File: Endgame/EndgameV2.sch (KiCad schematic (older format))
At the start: 160 parts, among them J1 OLED, SW1 Rotary_Encoder, SW2 SW_PUSH, U1 ATmega32U4-AU, U2 ai03-locallib_PRTR5V0U2X, Y1 Crystal_GND24_Small

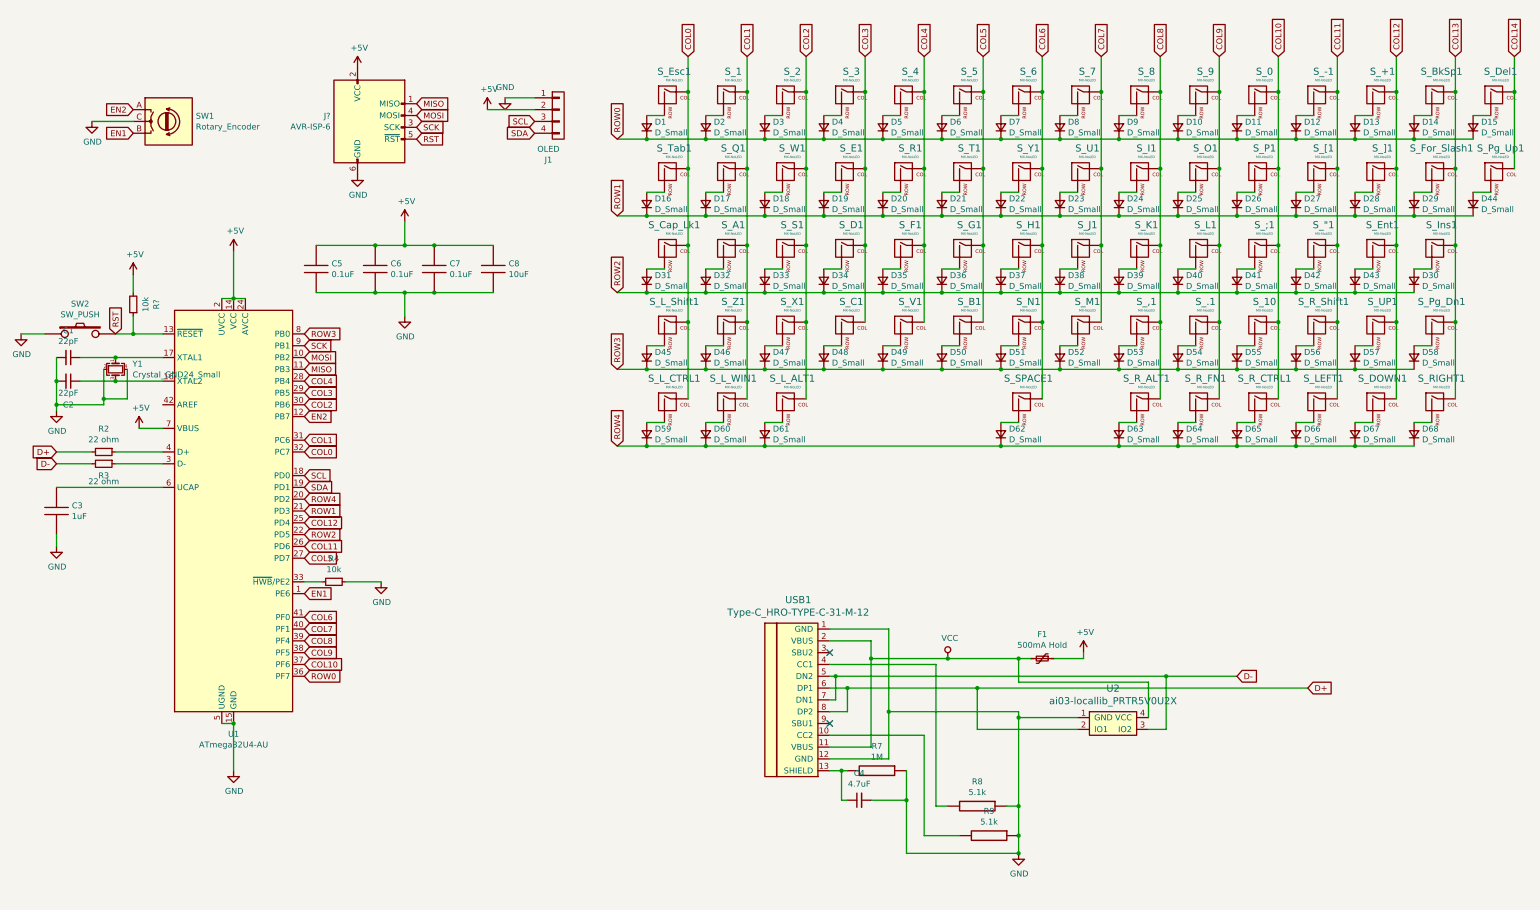
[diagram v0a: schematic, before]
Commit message: redrew key matrix
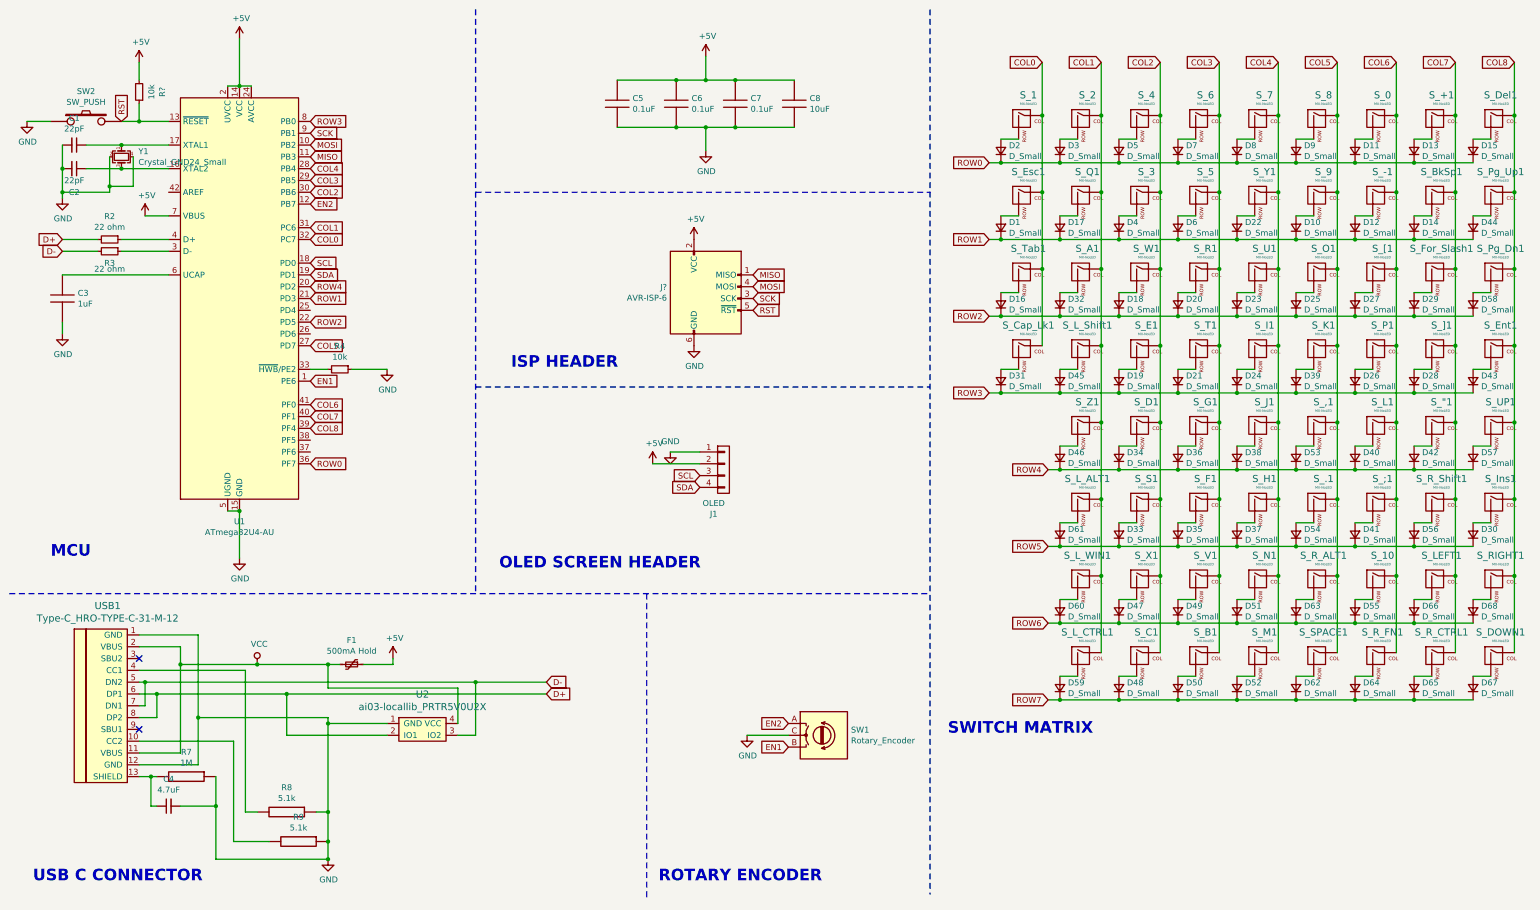
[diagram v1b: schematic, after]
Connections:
- net COL14 is gone; now on net COL8: S_Del1.1 (COL), S_Pg_Up1.1 (COL)
- net COL0: now also S_1.1 (COL); no longer S_L_CTRL1.1 (COL), S_L_Shift1.1 (COL)
- net COL1: now also S_2.1 (COL), S_L_ALT1.1 (COL), S_L_CTRL1.1 (COL), S_L_Shift1.1 (COL); no longer S_1.1 (COL)
- net COL2: now also S_3.1 (COL), S_4.1 (COL), S_C1.1 (COL), S_D1.1 (COL), S_E1.1 (COL); no longer S_2.1 (COL), S_L_ALT1.1 (COL)
- net COL3: now also S_5.1 (COL), S_6.1 (COL), S_B1.1 (COL), S_F1.1 (COL), S_G1.1 (COL), S_R1.1 (COL), S_T1.1 (COL), S_V1.1 (COL); no longer S_3.1 (COL), S_C1.1 (COL), S_D1.1 (COL), S_E1.1 (COL)
- net COL4: now also S_7.1 (COL), S_H1.1 (COL), S_I1.1 (COL), S_J1.1 (COL), S_M1.1 (COL), S_N1.1 (COL), S_U1.1 (COL), S_Y1.1 (COL); no longer S_4.1 (COL), S_F1.1 (COL), S_R1.1 (COL), S_V1.1 (COL)
- net COL5: now also S_,1.1 (COL), S_.1.1 (COL), S_8.1 (COL), S_9.1 (COL), S_K1.1 (COL), S_O1.1 (COL), S_R_ALT1.1 (COL), S_SPACE1.1 (COL); no longer S_5.1 (COL), S_B1.1 (COL), S_G1.1 (COL), S_T1.1 (COL)
- net COL6: now also S_-1.1 (COL), S_0.1 (COL), S_10.1 (COL), S_;1.1 (COL), S_L1.1 (COL), S_P1.1 (COL), S_R_FN1.1 (COL), S_[1.1 (COL); no longer S_6.1 (COL), S_H1.1 (COL), S_N1.1 (COL), S_SPACE1.1 (COL), S_Y1.1 (COL)
- net COL7: now also S_"1.1 (COL), S_+1.1 (COL), S_BkSp1.1 (COL), S_For_Slash1.1 (COL), S_LEFT1.1 (COL), S_R_CTRL1.1 (COL), S_R_Shift1.1 (COL), S_]1.1 (COL); no longer S_7.1 (COL), S_J1.1 (COL), S_M1.1 (COL), S_U1.1 (COL)
- net COL8: now also S_DOWN1.1 (COL), S_Ent1.1 (COL), S_Ins1.1 (COL), S_Pg_Dn1.1 (COL), S_RIGHT1.1 (COL), S_UP1.1 (COL); no longer S_,1.1 (COL), S_8.1 (COL), S_I1.1 (COL), S_K1.1 (COL), S_R_ALT1.1 (COL)
- net ROW0: no longer D1.1 (K), D10.1 (K), D12.1 (K), D14.1 (K), D4.1 (K), D6.1 (K)
- net ROW1: now also D1.1 (K), D10.1 (K), D12.1 (K), D14.1 (K), D4.1 (K), D6.1 (K); no longer D16.1 (K), D18.1 (K), D19.1 (K), D20.1 (K), D21.1 (K), D23.1 (K), D24.1 (K), D25.1 (K), D26.1 (K), D27.1 (K), D28.1 (K), D29.1 (K)
- net ROW2: now also D16.1 (K), D18.1 (K), D20.1 (K), D23.1 (K), D25.1 (K), D27.1 (K), D29.1 (K), D58.1 (K); no longer D30.1 (K), D31.1 (K), D33.1 (K), D34.1 (K), D35.1 (K), D36.1 (K), D37.1 (K), D38.1 (K), D39.1 (K), D40.1 (K), D41.1 (K), D42.1 (K), D43.1 (K)
- net ROW3: now also D19.1 (K), D21.1 (K), D24.1 (K), D26.1 (K), D28.1 (K), D31.1 (K), D39.1 (K), D43.1 (K); no longer D46.1 (K), D47.1 (K), D48.1 (K), D49.1 (K), D50.1 (K), D51.1 (K), D52.1 (K), D53.1 (K), D54.1 (K), D55.1 (K), D56.1 (K), D57.1 (K), D58.1 (K)
- net ROW4: now also D34.1 (K), D36.1 (K), D38.1 (K), D40.1 (K), D42.1 (K), D46.1 (K), D53.1 (K), D57.1 (K); no longer D59.1 (K), D60.1 (K), D61.1 (K), D62.1 (K), D63.1 (K), D64.1 (K), D65.1 (K), D66.1 (K), D67.1 (K), D68.1 (K)
- removed net COL10: S_0.1 (COL), S_10.1 (COL), S_;1.1 (COL), S_P1.1 (COL), S_R_CTRL1.1 (COL), U1.37 (PF6)
- removed net COL11: S_"1.1 (COL), S_-1.1 (COL), S_LEFT1.1 (COL), S_R_Shift1.1 (COL), S_[1.1 (COL), U1.26 (PD6)
- removed net COL12: S_+1.1 (COL), S_DOWN1.1 (COL), S_Ent1.1 (COL), S_UP1.1 (COL), S_]1.1 (COL), U1.25 (PD4)
- removed net COL13: S_BkSp1.1 (COL), S_For_Slash1.1 (COL), S_Ins1.1 (COL), S_Pg_Dn1.1 (COL), S_RIGHT1.1 (COL)
- removed net COL9: S_.1.1 (COL), S_9.1 (COL), S_L1.1 (COL), S_O1.1 (COL), S_R_FN1.1 (COL), U1.38 (PF5)
- new net ROW5: D30.1 (K), D33.1 (K), D35.1 (K), D37.1 (K), D41.1 (K), D54.1 (K), D56.1 (K), D61.1 (K)
- new net ROW6: D47.1 (K), D49.1 (K), D51.1 (K), D55.1 (K), D60.1 (K), D63.1 (K), D66.1 (K), D68.1 (K)
- new net ROW7: D48.1 (K), D50.1 (K), D52.1 (K), D59.1 (K), D62.1 (K), D64.1 (K), D65.1 (K), D67.1 (K)
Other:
- note added: "ISP HEADER"
- note added: "MCU"
- note added: "OLED SCREEN HEADER"
- note added: "ROTARY ENCODER"
- note added: "SWITCH MATRIX"
- note added: "USB C CONNECTOR"
- moved on the sheet: C1, C2, C3, C4, C5, C6, C7, C8, D1, D10, D11, D12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

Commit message: USB retrace
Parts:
- J2: renamed from J?; footprint (none) -> Keebio-Parts:ICSP-Header
- gave numbers to parts that had none: 1
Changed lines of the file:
@@
 $EndComp
 Wire Wire Line
-	2400 750  2400 1150
+	2300 750  2300 1150
 Wire Wire Line
 	2500 1150 2400 1150
@@
 L power:+5V #PWR0108
 U 1 1 5DE865F8
-P 2400 750
-F 0 "#PWR0108" H 2400 600 50  0001 C CNN
-F 1 "+5V" H 2415 923 50  0000 C CNN
-F 2 "" H 2400 750 50  0001 C CNN
-F 3 "" H 2400 750 50  0001 C CNN
-	1    2400 750
+P 2300 750
+F 0 "#PWR0108" H 2300 600 50  0001 C CNN
+F 1 "+5V" H 2315 923 50  0000 C CNN
+F 2 "" H 2300 750 50  0001 C CNN
+F 3 "" H 2300 750 50  0001 C CNN
+	1    2300 750
 	1    0    0    -1
 $EndComp
@@
 	1400 2550 1800 2550
 $Comp
-L power:+5V #PWR?
+L power:+5V #PWR0106
 U 1 1 5DF42376
 P 5900 4350
-F 0 "#PWR?" H 5900 4200 50  0001 C CNN
+F 0 "#PWR0106" H 5900 4200 50  0001 C CNN
 F 1 "+5V" H 5915 4523 50  0000 C CNN
 F 2 "" H 5900 4350 50  0001 C CNN
@@
 	5900 4350 6300 4350
 $Comp
-L Device:R_Small R?
+L Device:R_Small R1
 U 1 1 5DE94258
 P 1550 1200
-F 0 "R?" V 1354 1200 50  0000 C CNN
+F 0 "R1" V 1354 1200 50  0000 C CNN
 F 1 "10k" V 1445 1200 50  0000 C CNN
 F 2 "Resistor_SMD:R_0805_2012Metric" H 1550 1200 50  0001 C CNN
@@
 	1550 1450 1800 1450
 $Comp
-L power:+5V #PWR?
+L power:+5V #PWR0107
 U 1 1 5DE97BB7
 P 1550 950
-F 0 "#PWR?" H 1550 800 50  0001 C CNN
+F 0 "#PWR0107" H 1550 800 50  0001 C CNN
 F 1 "+5V" H 1565 1123 50  0000 C CNN
 F 2 "" H 1550 950 50  0001 C CNN
@@
 	1550 1100 1550 950
 $Comp
-L Connector:AVR-ISP-6 J?
+L Connector:AVR-ISP-6 J2
 U 1 1 5DF23484
 P 6350 2950
-F 0 "J?" H 6021 3046 50  0000 R CNN
+F 0 "J2" H 6021 3046 50  0000 R CNN
 F 1 "AVR-ISP-6" H 6021 2955 50  0000 R CNN
-F 2 "" V 6100 3000 50  0001 C CNN
+F 2 "Keebio-Parts:ICSP-Header" V 6100 3000 50  0001 C CNN
 F 3 " ~" H 5075 2400 50  0001 C CNN
 	1    6350 2950
@@
 RST
 $Comp
-L power:+5V #PWR?
+L power:+5V #PWR0117
 U 1 1 5DF4285F
 P 6250 2450
-F 0 "#PWR?" H 6250 2300 50  0001 C CNN
+F 0 "#PWR0117" H 6250 2300 50  0001 C CNN
 F 1 "+5V" H 6265 2623 50  0000 C CNN
 F 2 "" H 6250 2450 50  0001 C CNN
@@
 $EndComp
 $Comp
-L power:GND #PWR?
+L power:GND #PWR0118
 U 1 1 5DF44397
 P 6250 3350
-F 0 "#PWR?" H 6250 3100 50  0001 C CNN
+F 0 "#PWR0118" H 6250 3100 50  0001 C CNN
 F 1 "GND" H 6255 3177 50  0000 C CNN
 F 2 "" H 6250 3350 50  0001 C CNN
@@
 Text Notes 5950 7900 0    98   ~ 20
 ROTARY ENCODER
+Connection ~ 2300 1150
+Text Label 1600 1450 0    98   ~ 20
+RST
 $EndSCHEMATC
